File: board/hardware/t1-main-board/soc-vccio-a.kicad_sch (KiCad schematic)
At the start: 2 parts, among them U1301 RK3566

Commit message: Board: capture blk.debug
Debug UART2 (1.8 V) and I2S/DSD pads with ground pads, reset, PMIC and
power-key pads (PCB-T-09), a pad on every spare SoC GPIO whose pinout v1
row names one (the DEBUG bus, on the SoC's right edge), and a rail pad
for each power-tree rail no other sheet probes (PCB-T-02). Each DAC
sheet carries a pad on its MCLK. The spares pinout v1 leaves without a
pad now carry no-connect flags. On the root, facing sheet pins are
joined directly only where the route meets no other symbol.

Co-Authored-By: Claude Opus 5.5 <noreply@anthropic.com>
Claude-Session: https://claude.ai/code/session_01Ei262h3TpgY9vyfNLMi5Mn
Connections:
- net SPARE_1D4: no longer names the net of U1301.1C15 (FSPI_D3/FLASH_CS1n/GPIO1_D4_u)
- no-connect marks 7 -> 8
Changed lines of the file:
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@@
 (wire (pts (xy 157.48 77.47) (xy 154.94 77.47)) (stroke (width 0) (type default)))
 (wire (pts (xy 157.48 80.01) (xy 154.94 80.01)) (stroke (width 0) (type default)))
-(wire (pts (xy 157.48 82.55) (xy 154.94 82.55)) (stroke (width 0) (type default)))
+(no_connect (at 157.48 82.55))
 (symbol (lib_id "Rockchip:RK3566") (at 287.02 49.53 0) (unit 8) (body_style 1) (exclude_from_sim no) (in_bom yes) (on_board yes) (dnp no)
   (property "Reference" "U1301" (at 252.73 35.56 0) (effects (font (size 1.27 1.27)) (justify left)))
@@
 (label "SPARE_1D1" (at 154.94 77.47 180) (effects (font (size 1.27 1.27)) (justify right bottom)))
 (label "TPM_PIRQ_N" (at 154.94 80.01 180) (effects (font (size 1.27 1.27)) (justify right bottom)))
-(label "SPARE_1D4" (at 154.94 82.55 180) (effects (font (size 1.27 1.27)) (justify right bottom)))
 (label "SD_CLK" (at 243.84 41.91 180) (effects (font (size 1.27 1.27)) (justify right bottom)))
 (label "SD_CMD" (at 243.84 44.45 180) (effects (font (size 1.27 1.27)) (justify right bottom)))
@@
 (label "TPM_PIRQ_N" (at 38.1 186.69 270) (effects (font (size 1.27 1.27)) (justify right bottom)))
 (bus (pts (xy 45.72 270.51) (xy 50.8 270.51)) (stroke (width 0) (type default)))
-(hierarchical_label "{EMMC}" (shape bidirectional) (at 45.72 270.51 180) (effects (font (size 1.27 1.27)) (justify right)))
+(hierarchical_label "{DEBUG}" (shape bidirectional) (at 45.72 270.51 180) (effects (font (size 1.27 1.27)) (justify right)))
 (bus (pts (xy 45.72 265.43) (xy 50.8 265.43)) (stroke (width 0) (type default)))
-(hierarchical_label "{NFC}" (shape bidirectional) (at 45.72 265.43 180) (effects (font (size 1.27 1.27)) (justify right)))
+(hierarchical_label "{EMMC}" (shape bidirectional) (at 45.72 265.43 180) (effects (font (size 1.27 1.27)) (justify right)))
 (bus (pts (xy 45.72 260.35) (xy 50.8 260.35)) (stroke (width 0) (type default)))
-(hierarchical_label "{RP}" (shape bidirectional) (at 45.72 260.35 180) (effects (font (size 1.27 1.27)) (justify right)))
+(hierarchical_label "{NFC}" (shape bidirectional) (at 45.72 260.35 180) (effects (font (size 1.27 1.27)) (justify right)))
 (bus (pts (xy 45.72 255.27) (xy 50.8 255.27)) (stroke (width 0) (type default)))
-(hierarchical_label "{SDMMC0}" (shape bidirectional) (at 45.72 255.27 180) (effects (font (size 1.27 1.27)) (justify right)))
+(hierarchical_label "{RP}" (shape bidirectional) (at 45.72 255.27 180) (effects (font (size 1.27 1.27)) (justify right)))
 (bus (pts (xy 45.72 250.19) (xy 50.8 250.19)) (stroke (width 0) (type default)))
-(hierarchical_label "{TPM}" (shape bidirectional) (at 45.72 250.19 180) (effects (font (size 1.27 1.27)) (justify right)))
+(hierarchical_label "{SDMMC0}" (shape bidirectional) (at 45.72 250.19 180) (effects (font (size 1.27 1.27)) (justify right)))
 (bus (pts (xy 45.72 245.11) (xy 50.8 245.11)) (stroke (width 0) (type default)))
-(hierarchical_label "{WL}" (shape bidirectional) (at 45.72 245.11 180) (effects (font (size 1.27 1.27)) (justify right)))
+(hierarchical_label "{TPM}" (shape bidirectional) (at 45.72 245.11 180) (effects (font (size 1.27 1.27)) (justify right)))
+(bus (pts (xy 45.72 240.03) (xy 50.8 240.03)) (stroke (width 0) (type default)))
+(hierarchical_label "{WL}" (shape bidirectional) (at 45.72 240.03 180) (effects (font (size 1.27 1.27)) (justify right)))
 (embedded_fonts no))

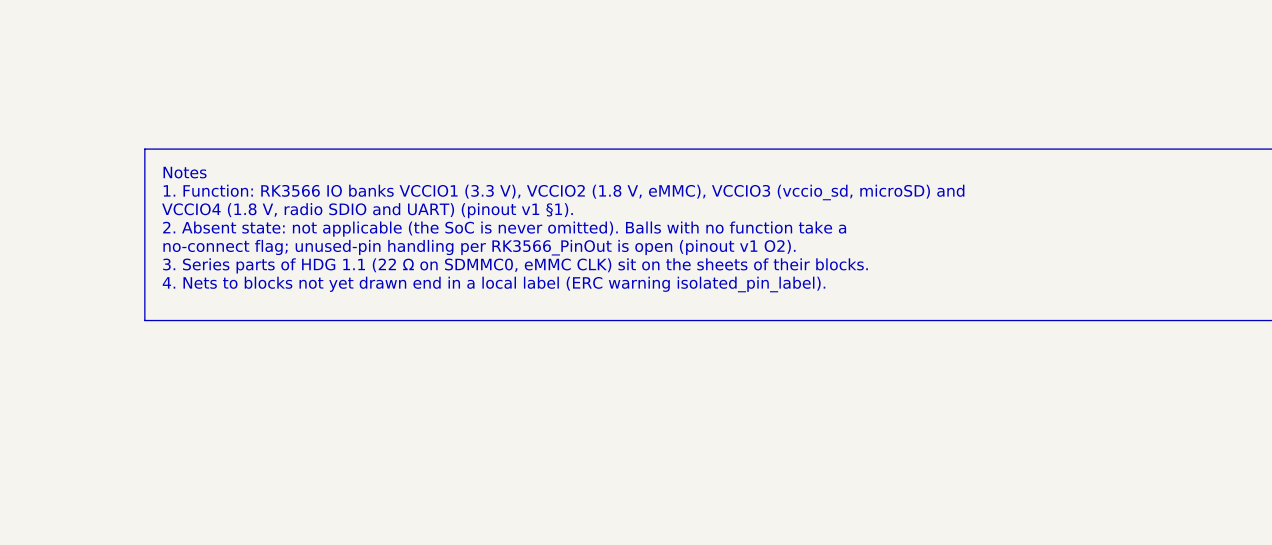
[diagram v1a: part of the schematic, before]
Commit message: Board: capture blk.maskrom
Power + Vol- at a cold power-on pull eMMC D0 low inside the TPS3808G01
boot window (BOM v1 lines 35, 78, 97, 98; sim/maskrom): SENSE 280k/100k,
CT 390 nF, WINDOW_N with its pad, SN74LVC1G57 and SN74LVC1G58 on
vcca1v8_pmu, BAT54 from PWRON_N, DMG1012T through 1 kΩ to EMMC_D0.
Every block in use now has its sheet; the README states the remaining
single-pin nets.

Co-Authored-By: Claude Opus 5.5 <noreply@anthropic.com>
Claude-Session: https://claude.ai/code/session_01Ei262h3TpgY9vyfNLMi5Mn
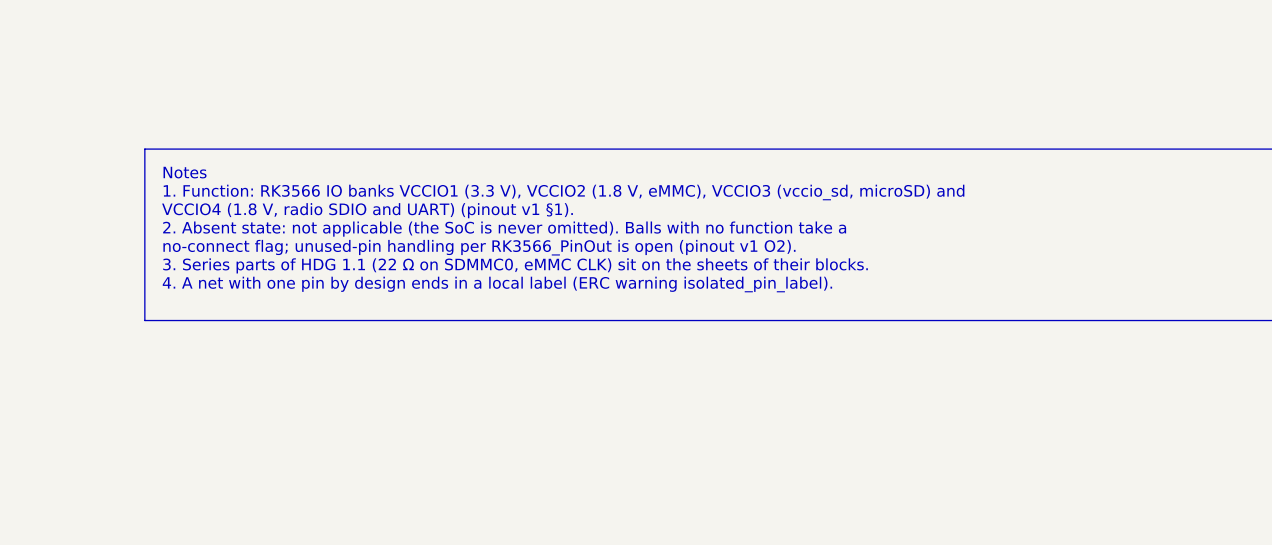
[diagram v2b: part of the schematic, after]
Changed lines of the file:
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@@
 )
 (wire (pts (xy 38.1 184.15) (xy 38.1 186.69)) (stroke (width 0) (type default)))
-(text_box "Notes\n1. Function: RK3566 IO banks VCCIO1 (3.3 V), VCCIO2 (1.8 V, eMMC), VCCIO3 (vccio_sd, microSD) and\n   VCCIO4 (1.8 V, radio SDIO and UART) (pinout v1 §1).\n2. Absent state: not applicable (the SoC is never omitted). Balls with no function take a\n   no-connect flag; unused-pin handling per RK3566_PinOut is open (pinout v1 O2).\n3. Series parts of HDG 1.1 (22 Ω on SDMMC0, eMMC CLK) sit on the sheets of their blocks.\n4. Nets to blocks not yet drawn end in a local label (ERC warning isolated_pin_label)." (exclude_from_sim no) (at 275.59 229.87 0) (size 129.54 19.05) (margins 1.905 1.905 1.905 1.905) (stroke (width 0) (type default)) (fill (type none)) (effects (font (size 1.27 1.27)) (justify left top)))
+(text_box "Notes\n1. Function: RK3566 IO banks VCCIO1 (3.3 V), VCCIO2 (1.8 V, eMMC), VCCIO3 (vccio_sd, microSD) and\n   VCCIO4 (1.8 V, radio SDIO and UART) (pinout v1 §1).\n2. Absent state: not applicable (the SoC is never omitted). Balls with no function take a\n   no-connect flag; unused-pin handling per RK3566_PinOut is open (pinout v1 O2).\n3. Series parts of HDG 1.1 (22 Ω on SDMMC0, eMMC CLK) sit on the sheets of their blocks.\n4. A net with one pin by design ends in a local label (ERC warning isolated_pin_label)." (exclude_from_sim no) (at 275.59 229.87 0) (size 129.54 19.05) (margins 1.905 1.905 1.905 1.905) (stroke (width 0) (type default)) (fill (type none)) (effects (font (size 1.27 1.27)) (justify left top)))
 (label "SPARE_1A1" (at 36.83 41.91 180) (effects (font (size 1.27 1.27)) (justify right bottom)))
 (label "SPARE_1A0" (at 36.83 44.45 180) (effects (font (size 1.27 1.27)) (justify right bottom)))

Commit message: Board on libs v0.2.0: lower-case kebab vendor keys (HL-13)
The libs submodule moves to v0.2.0 (5f24483). Every library nickname in
the generator, the placement tool and the floorplan study follows the
key table (Texas_Instruments -> texas-instruments, OpenDAP_Device ->
opendap-generic, Rockchip and Rockchip_PMIC -> rockchip, ...); the
library tables are written from the files. Schematic and board
regenerated.

Checks: ERC 0 errors (warnings unchanged); DRC 0 errors, 605 warnings,
the same counts by type, schematic parity 0; every placement identical;
craft Q1 met; pcb tests pass; STEP export resolves every libs 3D model
(the 27 parts without a model are KiCad stock lands that have none).

Co-Authored-By: Claude Opus 5.5 <noreply@anthropic.com>
Claude-Session: https://claude.ai/code/session_01Ei262h3TpgY9vyfNLMi5Mn
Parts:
- U1301: footprint Rockchip:Rockchip_FCCSP-565L_15.5x14.4mm_P0.4mm_P0.65mm_Ball0.25mm_Pad0.25mm_NSMD -> rockchip:Rockchip_FCCSP-565L_15.5x14.4mm_P0.4mm_P0.65mm_Ball0.25mm_Pad0.25mm_NSMD; symbol Rockchip:RK3566 -> rockchip:RK3566
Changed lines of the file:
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@@
 (paper "A3")
 (title_block (title "SoC: VCCIO1 to VCCIO4") (date "2026-10-25") (rev "A") (company "The OpenDAP Project") (comment 1 "blk.soc-vccio-a") (comment 2 "RK3566 IO banks VCCIO1-4: eMMC, microSD, the radio SDIO and UART, and spare GPIO"))
-(symbol (lib_id "Rockchip:RK3566") (at 90.17 57.15 0) (unit 6) (body_style 1) (exclude_from_sim no) (in_bom yes) (on_board yes) (dnp no)
+(symbol (lib_id "rockchip:RK3566") (at 90.17 57.15 0) (unit 6) (body_style 1) (exclude_from_sim no) (in_bom yes) (on_board yes) (dnp no)
   (property "Reference" "U1301" (at 45.72 35.56 0) (effects (font (size 1.27 1.27)) (justify left)))
   (property "Value" "RK3566" (at 45.72 33.02 0) (effects (font (size 1.27 1.27)) (justify left)))
-  (property "Footprint" "Rockchip:Rockchip_FCCSP-565L_15.5x14.4mm_P0.4mm_P0.65mm_Ball0.25mm_Pad0.25mm_NSMD" (at 90.17 57.15 0) (effects (font (size 1.27 1.27))) (hide yes))
+  (property "Footprint" "rockchip:Rockchip_FCCSP-565L_15.5x14.4mm_P0.4mm_P0.65mm_Ball0.25mm_Pad0.25mm_NSMD" (at 90.17 57.15 0) (effects (font (size 1.27 1.27))) (hide yes))
   (property "Datasheet" "https://dl.xkwy2018.com/downloads/RK3568/Rockchip-RK3566-Datasheet-V1.1-20210305.pdf" (at 90.17 57.15 0) (effects (font (size 1.27 1.27))) (hide yes))
   (property "Description" "Quad-core Arm Cortex-A55 application processor, LPDDR4X/DDR4 32-bit, eMMC 5.1, FCCSP565L 15.5 x 14.4 mm" (at 90.17 57.15 0) (effects (font (size 1.27 1.27))) (hide yes))
@@
 (no_connect (at 39.37 67.31))
 (no_connect (at 39.37 69.85))
-(symbol (lib_id "Rockchip:RK3566") (at 195.58 62.23 0) (unit 7) (body_style 1) (exclude_from_sim no) (in_bom yes) (on_board yes) (dnp no)
+(symbol (lib_id "rockchip:RK3566") (at 195.58 62.23 0) (unit 7) (body_style 1) (exclude_from_sim no) (in_bom yes) (on_board yes) (dnp no)
   (property "Reference" "U1301" (at 163.83 35.56 0) (effects (font (size 1.27 1.27)) (justify left)))
   (property "Value" "RK3566" (at 163.83 33.02 0) (effects (font (size 1.27 1.27)) (justify left)))
-  (property "Footprint" "Rockchip:Rockchip_FCCSP-565L_15.5x14.4mm_P0.4mm_P0.65mm_Ball0.25mm_Pad0.25mm_NSMD" (at 195.58 62.23 0) (effects (font (size 1.27 1.27))) (hide yes))
+  (property "Footprint" "rockchip:Rockchip_FCCSP-565L_15.5x14.4mm_P0.4mm_P0.65mm_Ball0.25mm_Pad0.25mm_NSMD" (at 195.58 62.23 0) (effects (font (size 1.27 1.27))) (hide yes))
   (property "Datasheet" "https://dl.xkwy2018.com/downloads/RK3568/Rockchip-RK3566-Datasheet-V1.1-20210305.pdf" (at 195.58 62.23 0) (effects (font (size 1.27 1.27))) (hide yes))
   (property "Description" "Quad-core Arm Cortex-A55 application processor, LPDDR4X/DDR4 32-bit, eMMC 5.1, FCCSP565L 15.5 x 14.4 mm" (at 195.58 62.23 0) (effects (font (size 1.27 1.27))) (hide yes))
@@
 (wire (pts (xy 157.48 80.01) (xy 154.94 80.01)) (stroke (width 0) (type default)))
 (no_connect (at 157.48 82.55))
-(symbol (lib_id "Rockchip:RK3566") (at 287.02 49.53 0) (unit 8) (body_style 1) (exclude_from_sim no) (in_bom yes) (on_board yes) (dnp no)
+(symbol (lib_id "rockchip:RK3566") (at 287.02 49.53 0) (unit 8) (body_style 1) (exclude_from_sim no) (in_bom yes) (on_board yes) (dnp no)
   (property "Reference" "U1301" (at 252.73 35.56 0) (effects (font (size 1.27 1.27)) (justify left)))
   (property "Value" "RK3566" (at 252.73 33.02 0) (effects (font (size 1.27 1.27)) (justify left)))
-  (property "Footprint" "Rockchip:Rockchip_FCCSP-565L_15.5x14.4mm_P0.4mm_P0.65mm_Ball0.25mm_Pad0.25mm_NSMD" (at 287.02 49.53 0) (effects (font (size 1.27 1.27))) (hide yes))
+  (property "Footprint" "rockchip:Rockchip_FCCSP-565L_15.5x14.4mm_P0.4mm_P0.65mm_Ball0.25mm_Pad0.25mm_NSMD" (at 287.02 49.53 0) (effects (font (size 1.27 1.27))) (hide yes))
   (property "Datasheet" "https://dl.xkwy2018.com/downloads/RK3568/Rockchip-RK3566-Datasheet-V1.1-20210305.pdf" (at 287.02 49.53 0) (effects (font (size 1.27 1.27))) (hide yes))
   (property "Description" "Quad-core Arm Cortex-A55 application processor, LPDDR4X/DDR4 32-bit, eMMC 5.1, FCCSP565L 15.5 x 14.4 mm" (at 287.02 49.53 0) (effects (font (size 1.27 1.27))) (hide yes))
@@
 (wire (pts (xy 246.38 52.07) (xy 243.84 52.07)) (stroke (width 0) (type default)))
 (wire (pts (xy 246.38 54.61) (xy 243.84 54.61)) (stroke (width 0) (type default)))
-(symbol (lib_id "Rockchip:RK3566") (at 92.71 130.81 0) (unit 9) (body_style 1) (exclude_from_sim no) (in_bom yes) (on_board yes) (dnp no)
+(symbol (lib_id "rockchip:RK3566") (at 92.71 130.81 0) (unit 9) (body_style 1) (exclude_from_sim no) (in_bom yes) (on_board yes) (dnp no)
   (property "Reference" "U1301" (at 48.26 99.06 0) (effects (font (size 1.27 1.27)) (justify left)))
   (property "Value" "RK3566" (at 48.26 96.52 0) (effects (font (size 1.27 1.27)) (justify left)))
-  (property "Footprint" "Rockchip:Rockchip_FCCSP-565L_15.5x14.4mm_P0.4mm_P0.65mm_Ball0.25mm_Pad0.25mm_NSMD" (at 92.71 130.81 0) (effects (font (size 1.27 1.27))) (hide yes))
+  (property "Footprint" "rockchip:Rockchip_FCCSP-565L_15.5x14.4mm_P0.4mm_P0.65mm_Ball0.25mm_Pad0.25mm_NSMD" (at 92.71 130.81 0) (effects (font (size 1.27 1.27))) (hide yes))
   (property "Datasheet" "https://dl.xkwy2018.com/downloads/RK3568/Rockchip-RK3566-Datasheet-V1.1-20210305.pdf" (at 92.71 130.81 0) (effects (font (size 1.27 1.27))) (hide yes))
   (property "Description" "Quad-core Arm Cortex-A55 application processor, LPDDR4X/DDR4 32-bit, eMMC 5.1, FCCSP565L 15.5 x 14.4 mm" (at 92.71 130.81 0) (effects (font (size 1.27 1.27))) (hide yes))

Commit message: Board in the 62.5 x 95.0 mm body: ADR 0025, outline 59.1 x 91.6, 0201 swaps
ADR 0025 supersedes ADR 0016 for t1 ADR 0006's body: board outline from
the body, 1.2 mm walls and 0.5 mm clearance; height zones and stack
restated unchanged; the speaker on a case shelf (PCB-Z-09); pocket
reliefs at the 4.4 mm jack, the microSD (DM3AT push-push kept) and the
side buttons; the audio 0603 -> 0402 swap gated by t1 V2-A08; reserve
(NFC reader, then TPM) recorded, not applied.

- pcb/geometry.py derives the outline from BODY, WALL and CLEARANCE;
  the pocket, display and fixed parts keep their device-frame positions;
  holes keep their edge distance; the speaker shadow becomes a 1.5 mm
  shelf height area (placement, checks, occupancy).
- build.py reports pocket reliefs and routing room; C904 unfixed (it
  now finds back room, so PCB-Z-04 carries no part).
- Generator: parts.area_swap puts 121 generic 0402 resistors (outside
  audio and VBUS paths, >= 10 ohm) and five 100 nF signal capacitors in
  0201 (BOM v1.16); schematic and board regenerated.
- Result: 1,012/1,012 placed, 98.8 % by the floorplan method (was 111 %),
  factor left 1.68 (was 1.49); DRC 0 errors, ERC 0 errors, 0 check
  findings, pcb tests 20/20, schematic craft Q1 met.
- Specs: PCB constraints v0.17 (M-01, M-02, M-08, Z-02, Z-06 to Z-09,
  R-07), placement v1.1 (section 3, decisions 4 and 13, checks, open
  items with the gated swaps and the reserve), floorplan v1 section 1,
  BOM v1.16.

Co-Authored-By: Claude Opus 5.5 <noreply@anthropic.com>
Claude-Session: https://claude.ai/code/session_01Ei262h3TpgY9vyfNLMi5Mn
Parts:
- R1321: footprint Resistor_SMD:R_0402_1005Metric -> Resistor_SMD:R_0201_0603Metric; MPN RC0402FR-074K7L -> RC0201FR-074K7L
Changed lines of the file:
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@@
   (property "Reference" "R1321" (at 39.37 179.07 0) (effects (font (size 1.27 1.27)) (justify left)))
   (property "Value" "4.7 kΩ" (at 39.37 181.61 0) (effects (font (size 1.27 1.27)) (justify left)))
-  (property "Footprint" "Resistor_SMD:R_0402_1005Metric" (at 38.1 180.34 0) (effects (font (size 1.27 1.27))) (hide yes))
-  (property "Datasheet" "https://yageogroup.com/en/ProductSearch/PartNumberSearch?part=RC0402FR-074K7L" (at 38.1 180.34 0) (effects (font (size 1.27 1.27))) (hide yes))
-  (property "Description" "Resistor, 4.7 kΩ, 1 %, 1/16 W, 0402" (at 38.1 180.34 0) (effects (font (size 1.27 1.27))) (hide yes))
+  (property "Footprint" "Resistor_SMD:R_0201_0603Metric" (at 38.1 180.34 0) (effects (font (size 1.27 1.27))) (hide yes))
+  (property "Datasheet" "https://yageogroup.com/en/ProductSearch/PartNumberSearch?part=RC0201FR-074K7L" (at 38.1 180.34 0) (effects (font (size 1.27 1.27))) (hide yes))
+  (property "Description" "Resistor, 4.7 kΩ, 1 %, 1/20 W, 0201" (at 38.1 180.34 0) (effects (font (size 1.27 1.27))) (hide yes))
   (property "Manufacturer" "YAGEO" (at 38.1 180.34 0) (effects (font (size 1.27 1.27))) (hide yes))
-  (property "MPN" "RC0402FR-074K7L" (at 38.1 180.34 0) (effects (font (size 1.27 1.27))) (hide yes))
+  (property "MPN" "RC0201FR-074K7L" (at 38.1 180.34 0) (effects (font (size 1.27 1.27))) (hide yes))
   (property "Block" "blk.soc-vccio-a" (at 38.1 180.34 0) (effects (font (size 1.27 1.27))) (hide yes))
   (pin "1")

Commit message: NFC reader withdrawn from the board, every model (BRD-057)
Maintainer decision 2026-10-27, reason: board area. blk.nfc-reader (#42)
withdrawn: PN7160, front end, crystal, antenna contacts, NFC_VBAT switch
and link #18 removed (35 parts). BRD-057 reworded: NFC as the dynamic tag
only; blk.nfc-tag stays. Pinout v1: 1N20, A37, B38 become unconnected
spares, expander P05 a spare. BOM v1.18 item 7 (line 50: 5 switches,
lines 127-128 withdrawn), power tree v0.10, variant files, feature blocks.

Sheets after the removed one move up a page; references renumbered in
plan.py, parts.py and the specs (J6201 -> J6101 and others).

Placement v1.4: 990 parts placed, board need 96.9 % (99.1 % before),
factor 1.72; 243 capacitors within bound; DRC 0 errors; ERC 0 errors;
craft Q1 met; overlaps 0; pcb tests pass; STEP exported.

Co-Authored-By: Claude Opus 5.5 <noreply@anthropic.com>
Claude-Session: https://claude.ai/code/session_01Ei262h3TpgY9vyfNLMi5Mn
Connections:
- net NFC_DWL_REQ: no longer names the net of U1301.B38 (CLK32K_OUT1/UART8_RX_M0/SPI1_CS1_M0/GPIO2_C6_d)
- net NFC_VEN: no longer names the net of U1301.A37 (I2S2_LRCK_RX_M0/UART6_CTSn_M0/SPI1_CS0_M0/GPIO2_C0_d)
- no-connect marks 8 -> 10
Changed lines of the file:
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@@
   (instances (project "t1-main-board" (path "/7746052e-d7f9-59ad-ba73-bd2b74439529/8302eaa7-1fc9-5a34-8a84-8a9171d22bdf/174ad081-00db-56fe-bc29-230aaabeb10b" (reference "U1301") (unit 9))))
 )
-(wire (pts (xy 41.91 105.41) (xy 39.37 105.41)) (stroke (width 0) (type default)))
-(wire (pts (xy 41.91 107.95) (xy 39.37 107.95)) (stroke (width 0) (type default)))
+(no_connect (at 41.91 105.41))
+(no_connect (at 41.91 107.95))
 (no_connect (at 41.91 110.49))
 (no_connect (at 41.91 113.03))
@@
 (label "SD_D2" (at 243.84 52.07 180) (effects (font (size 1.27 1.27)) (justify right bottom)))
 (label "SD_D3" (at 243.84 54.61 180) (effects (font (size 1.27 1.27)) (justify right bottom)))
-(label "NFC_DWL_REQ" (at 39.37 105.41 180) (effects (font (size 1.27 1.27)) (justify right bottom)))
-(label "NFC_VEN" (at 39.37 107.95 180) (effects (font (size 1.27 1.27)) (justify right bottom)))
 (label "SPARE_2B7" (at 39.37 115.57 180) (effects (font (size 1.27 1.27)) (justify right bottom)))
 (label "BT_WAKE_IN" (at 39.37 120.65 180) (effects (font (size 1.27 1.27)) (justify right bottom)))
@@
 (hierarchical_label "{EMMC}" (shape bidirectional) (at 45.72 265.43 180) (effects (font (size 1.27 1.27)) (justify right)))
 (bus (pts (xy 45.72 260.35) (xy 50.8 260.35)) (stroke (width 0) (type default)))
-(hierarchical_label "{NFC}" (shape bidirectional) (at 45.72 260.35 180) (effects (font (size 1.27 1.27)) (justify right)))
+(hierarchical_label "{RP}" (shape bidirectional) (at 45.72 260.35 180) (effects (font (size 1.27 1.27)) (justify right)))
 (bus (pts (xy 45.72 255.27) (xy 50.8 255.27)) (stroke (width 0) (type default)))
-(hierarchical_label "{RP}" (shape bidirectional) (at 45.72 255.27 180) (effects (font (size 1.27 1.27)) (justify right)))
+(hierarchical_label "{SDMMC0}" (shape bidirectional) (at 45.72 255.27 180) (effects (font (size 1.27 1.27)) (justify right)))
 (bus (pts (xy 45.72 250.19) (xy 50.8 250.19)) (stroke (width 0) (type default)))
-(hierarchical_label "{SDMMC0}" (shape bidirectional) (at 45.72 250.19 180) (effects (font (size 1.27 1.27)) (justify right)))
+(hierarchical_label "{TPM}" (shape bidirectional) (at 45.72 250.19 180) (effects (font (size 1.27 1.27)) (justify right)))
 (bus (pts (xy 45.72 245.11) (xy 50.8 245.11)) (stroke (width 0) (type default)))
-(hierarchical_label "{TPM}" (shape bidirectional) (at 45.72 245.11 180) (effects (font (size 1.27 1.27)) (justify right)))
-(bus (pts (xy 45.72 240.03) (xy 50.8 240.03)) (stroke (width 0) (type default)))
-(hierarchical_label "{WL}" (shape bidirectional) (at 45.72 240.03 180) (effects (font (size 1.27 1.27)) (justify right)))
+(hierarchical_label "{WL}" (shape bidirectional) (at 45.72 245.11 180) (effects (font (size 1.27 1.27)) (justify right)))
 (embedded_fonts no))
